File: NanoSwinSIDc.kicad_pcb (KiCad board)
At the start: 2 copper layers, 17.8 x 36.6 mm, 15 parts, among them J1 JTAG, U1 C64-SID-Socket, U2 ATMEGA88PA-AU, X1 32Mhz

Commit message: Oscillator should have had a hand-soldering footprint.
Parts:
- X1: footprint Oscillators:Oscillator_SMD_EuroQuartz_XO53-4pin_5.0x3.2mm -> Oscillators:Oscillator_SMD_EuroQuartz_XO53-4pin_5.0x3.2mm_HandSoldering
- moved X1 0.52 mm to (133.8, 111.8)
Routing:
- net VCC: track 65.6 -> 67.1 mm
- net GND: vias 11 -> 12
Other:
- board text added: "Rev.2"
- board text removed: "Rev.1"

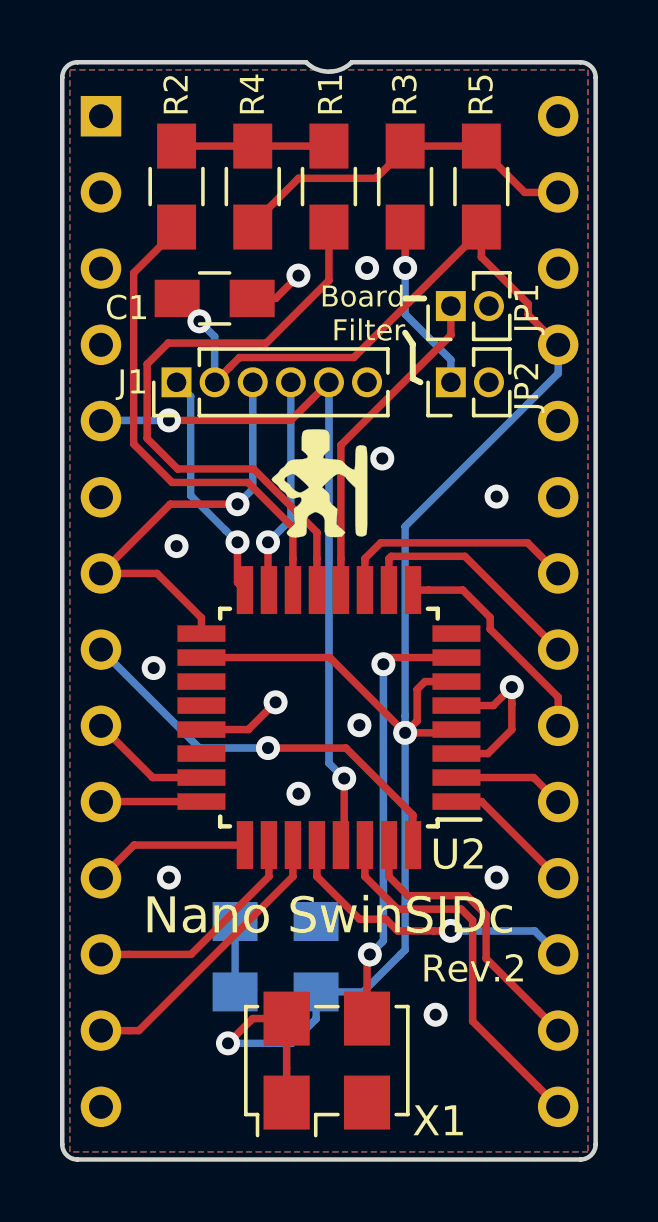
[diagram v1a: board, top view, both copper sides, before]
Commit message: Corrected jumper labels.
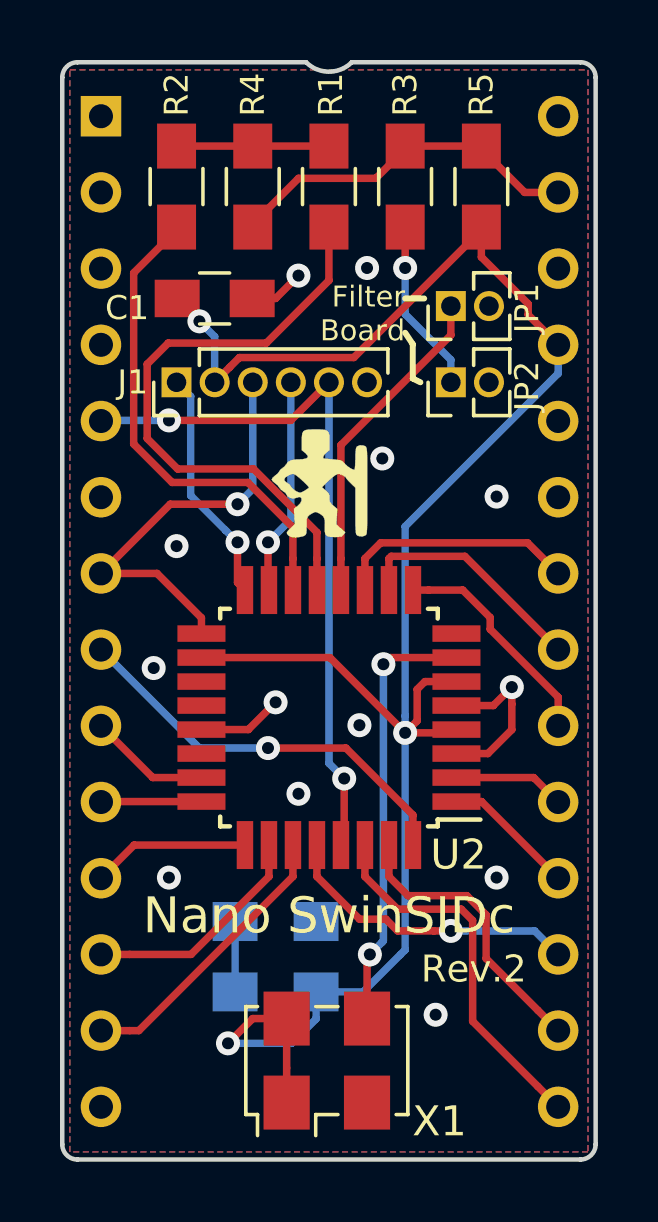
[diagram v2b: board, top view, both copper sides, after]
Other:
- board text added: "Filter Board"
- board text removed: "Board Filter"
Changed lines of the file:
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@@
   )
   (layers
-    (0 F.Cu signal)
-    (31 B.Cu signal)
+    (0 F.Cu signal hide)
+    (31 B.Cu signal hide)
     (32 B.Adhes user)
     (33 F.Adhes user)
@@
   (gr_line (start 136.398 87.503) (end 136.652 87.884) (layer F.SilkS) (width 0.2))
   (gr_line (start 136.398 86.36) (end 137.033 86.36) (layer F.SilkS) (width 0.2))
-  (gr_text "Board\nFilter" (at 136.398 86.868) (layer F.SilkS)
+  (gr_text "Filter\nBoard\n" (at 136.398 86.868) (layer F.SilkS)
     (effects (font (size 0.7 0.7) (thickness 0.15)) (justify right))
   )

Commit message: Replaced 50mil header with regular 100mil ones and adapted board layout.
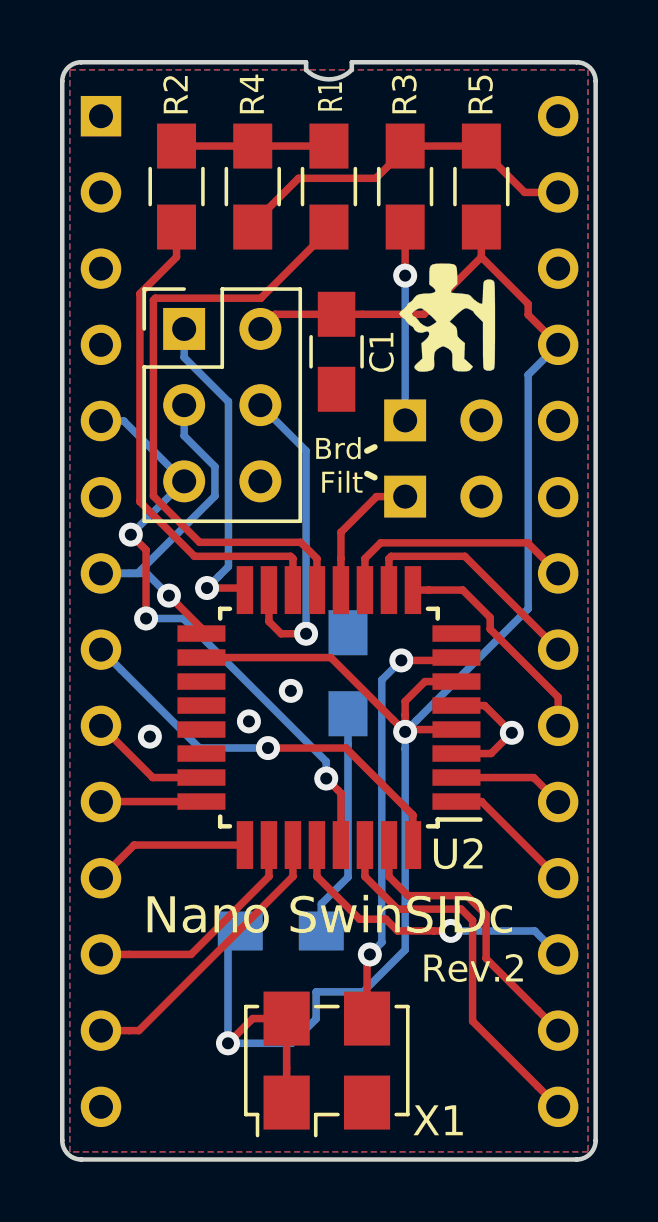
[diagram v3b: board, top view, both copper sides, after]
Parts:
- J1: footprint Pin_Headers:Pin_Header_Straight_1x06_Pitch1.27mm -> Pin_Headers:Pin_Header_Straight_2x03_Pitch2.54mm
- JP1, JP2: footprint Pin_Headers:Pin_Header_Straight_1x02_Pitch1.27mm -> Pin_Headers:Pin_Header_Angled_1x02_Pitch2.54mm
- moved D1 8.62 mm to (134.5, 98.9), turned to 270 degrees
- moved G*** 6.97 mm to (137.9, 86.9)
- moved JP1 6.53 mm to (136.4, 93.0)
- moved C1 4.44 mm to (134.1, 88.1), turned to 270 degrees
- moved R6 2.04 mm to (132.3, 107.4), turned to 0 degrees
- moved JP2 1.98 mm to (136.4, 90.4)
- moved J1 1.80 mm to (129.0, 87.4), turned to 0 degrees
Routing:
- net Net-(JP1-Pad1): track 11.0 -> 4.56 mm
- net GND: track 10.4 -> 4.35 mm, vias 12 -> 4
- net Net-(D1-Pad2): track 2.34 -> 7.61 mm
- net RESET: track 23.8 -> 20.1 mm, vias 2 -> 3
- net MOSI: track 7.25 -> 10.7 mm
- net MISO: track 7.87 -> 10.8 mm
- net VCC: track 67.1 -> 64.9 mm, vias 3 -> 2
- net SCK: track 14.3 -> 12.6 mm
- net Net-(JP2-Pad1): track 5.81 -> 6.44 mm
- net (no net): vias 1 -> 0
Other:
- outline, holes or cut-outs redrawn
- board text added: "Brd Filt"
- board text added: "github.com /hackup /NanoSwinSIDc"
- board text removed: "Filter Board"
- board text removed: "github.com/hackup/NanoSwinSIDc"

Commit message: Library update.
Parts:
- moved G*** 26.2 mm to (129.0, 111.6)
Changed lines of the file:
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@@
-(kicad_pcb (version 20171130) (host pcbnew "(5.0.0-rc2-dev-406-g05dae9627)")
+(kicad_pcb (version 20171130) (host pcbnew "(5.1.0)-1")
   (general
     (thickness 1.6)
@@
     (zone_45_only no)
     (trace_min 0.2)
-    (segment_width 0.2)
-    (edge_width 0.15)
     (via_size 0.8)
     (via_drill 0.4)
@@
     (uvia_min_size 0.2)
     (uvia_min_drill 0.1)
+    (edge_width 0.15)
+    (segment_width 0.2)
     (pcb_text_width 0.3)
     (pcb_text_size 1.5 1.5)
@@
       (hpglpennumber 1)
       (hpglpenspeed 20)
-      (hpglpendiameter 15)
+      (hpglpendiameter 15.000000)
       (psnegative false)
       (psa4output false)
@@
       (drillshape 0)
       (scaleselection 1)
-      (outputdirectory gerber/))
+      (outputdirectory "gerber/"))
   )
   (net 0 "")
@@
   )
   (module Logo:bigby2 (layer F.Cu)
-    (at 137.8585 86.9315)
+    (at 129.032 111.633)
     (fp_text reference G*** (at 0 0) (layer F.SilkS) hide
       (effects (font (size 1.524 1.524) (thickness 0.3)))
